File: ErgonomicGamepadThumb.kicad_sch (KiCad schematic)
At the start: 7 parts, among them J4 Conn_01x05, SW1 SW_DIP_x01, SW2 SW_DIP_x01, SW4 SW_DIP_x01

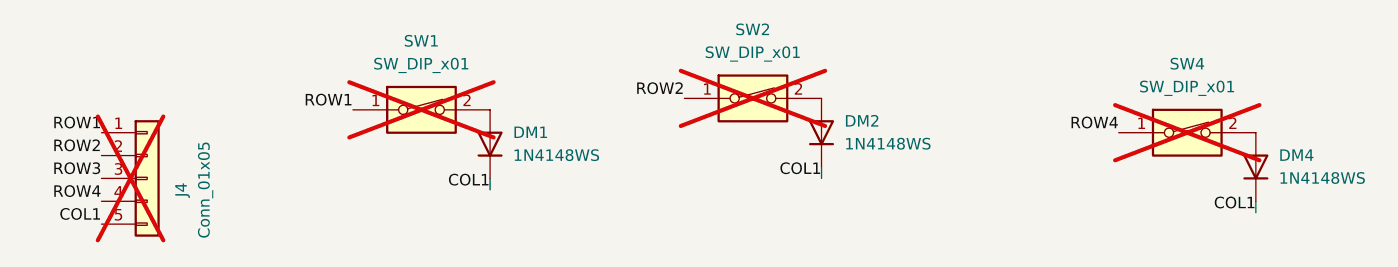
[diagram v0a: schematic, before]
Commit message: Continue ergonomic key stagger adjustments across satellite sheets
Update the layout-mirror script to read symbol positions from every
kicad_sch in the project, since the key matrix now lives across the
Pinkie/Thumb satellite sheets rather than a single top-level sheet.
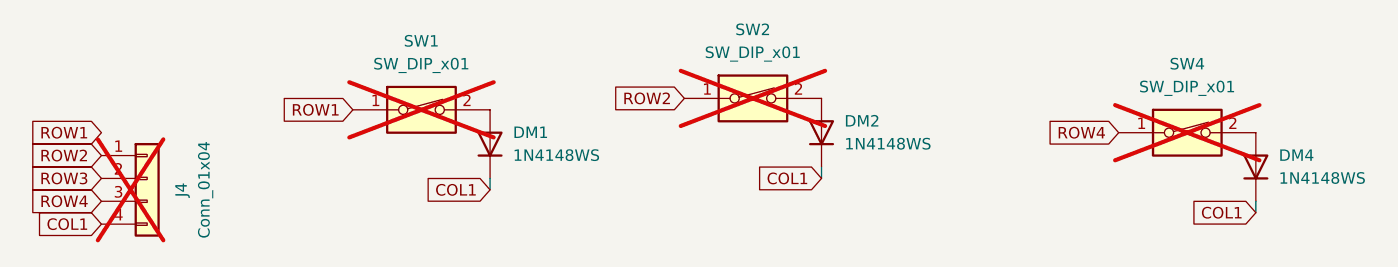
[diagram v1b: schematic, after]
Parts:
- J4: value Conn_01x05 -> Conn_01x04; footprint Connector_JST:JST_XH_B5B-XH-A_1x05_P2.50mm_Vertical -> Connector_JST:JST_XH_B4B-XH-A_1x04_P2.50mm_Vertical; symbol Connector_Generic:Conn_01x05 -> Connector_Generic:Conn_01x04; LCSC C157991 -> C144395; MPN B5B-XH-A(LF)(SN) -> B4B-XH-A(LF)(SN)
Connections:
- net COL1: now also J4.4 (Pin_4); no longer J4.5 (Pin_5)
- net ROW1: no longer J4.1 (Pin_1)
- net ROW2: now also J4.1 (Pin_1); no longer J4.2 (Pin_2)
- net ROW3: now also J4.2 (Pin_2); no longer J4.3 (Pin_3)
- net ROW4: now also J4.3 (Pin_3); no longer J4.4 (Pin_4)
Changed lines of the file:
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@@
 		)
 	)
-	(label "ROW4"
+	(global_label "ROW4"
+		(shape input)
 		(at 81.28 93.98 180)
-		(effects
-			(font
-				(size 1.27 1.27)
-			)
-			(justify right bottom)
-		)
-	)
-	(label "ROW3"
+		(fields_autoplaced yes)
+		(effects
+			(font
+				(size 1.27 1.27)
+			)
+			(justify right bottom)
+		)
+		(property "Intersheetrefs" "${INTERSHEET_REFS}"
+			(at 81.28 93.98 180)
+			(hide yes)
+			(show_name no)
+			(do_not_autoplace no)
+			(effects
+				(font
+					(size 1.27 1.27)
+				)
+				(justify right bottom)
+			)
+		)
+	)
+	(global_label "ROW3"
+		(shape input)
 		(at 81.28 91.44 180)
-		(effects
-			(font
-				(size 1.27 1.27)
-			)
-			(justify right bottom)
-		)
-	)
-	(label "COL1"
+		(fields_autoplaced yes)
+		(effects
+			(font
+				(size 1.27 1.27)
+			)
+			(justify right bottom)
+		)
+		(property "Intersheetrefs" "${INTERSHEET_REFS}"
+			(at 81.28 91.44 180)
+			(hide yes)
+			(show_name no)
+			(do_not_autoplace no)
+			(effects
+				(font
+					(size 1.27 1.27)
+				)
+				(justify right bottom)
+			)
+		)
+	)
+	(global_label "COL1"
+		(shape input)
 		(at 124.46 92.71 180)
-		(effects
-			(font
-				(size 1.27 1.27)
-			)
-			(justify right bottom)
-		)
-	)
-	(label "COL1"
+		(fields_autoplaced yes)
+		(effects
+			(font
+				(size 1.27 1.27)
+			)
+			(justify right bottom)
+		)
+		(property "Intersheetrefs" "${INTERSHEET_REFS}"
+			(at 124.46 92.71 180)
+			(hide yes)
+			(show_name no)
+			(do_not_autoplace no)
+			(effects
+				(font
+					(size 1.27 1.27)
+				)
+				(justify right bottom)
+			)
+		)
+	)
+	(global_label "COL1"
+		(shape input)
 		(at 81.28 96.52 180)
-		(effects
-			(font
-				(size 1.27 1.27)
-			)
-			(justify right bottom)
-		)
-	)
-	(label "ROW2"
+		(fields_autoplaced yes)
+		(effects
+			(font
+				(size 1.27 1.27)
+			)
+			(justify right bottom)
+		)
+		(property "Intersheetrefs" "${INTERSHEET_REFS}"
+			(at 81.28 96.52 180)
+			(hide yes)
+			(show_name no)
+			(do_not_autoplace no)
+			(effects
+				(font
+					(size 1.27 1.27)
+				)
+				(justify right bottom)
+			)
+		)
+	)
+	(global_label "ROW2"
+		(shape input)
 		(at 146.05 82.55 180)
-		(effects
-			(font
-				(size 1.27 1.27)
-			)
-			(justify right bottom)
-		)
-	)
-	(label "ROW1"
+		(fields_autoplaced yes)
+		(effects
+			(font
+				(size 1.27 1.27)
+			)
+			(justify right bottom)
+		)
+		(property "Intersheetrefs" "${INTERSHEET_REFS}"
+			(at 146.05 82.55 180)
+			(hide yes)
+			(show_name no)
+			(do_not_autoplace no)
+			(effects
+				(font
+					(size 1.27 1.27)
+				)
+				(justify right bottom)
+			)
+		)
+	)
+	(global_label "ROW1"
+		(shape input)
 		(at 81.28 86.36 180)
-		(effects
-			(font
-				(size 1.27 1.27)
-			)
-			(justify right bottom)
-		)
-	)
-	(label "COL1"
+		(fields_autoplaced yes)
+		(effects
+			(font
+				(size 1.27 1.27)
+			)
+			(justify right bottom)
+		)
+		(property "Intersheetrefs" "${INTERSHEET_REFS}"
+			(at 81.28 86.36 180)
+			(hide yes)
+			(show_name no)
+			(do_not_autoplace no)
+			(effects
+				(font
+					(size 1.27 1.27)
+				)
+				(justify right bottom)
+			)
+		)
+	)
+	(global_label "COL1"
+		(shape input)
 		(at 209.55 95.25 180)
-		(effects
-			(font
-				(size 1.27 1.27)
-			)
-			(justify right bottom)
-		)
-	)
-	(label "ROW4"
+		(fields_autoplaced yes)
+		(effects
+			(font
+				(size 1.27 1.27)
+			)
+			(justify right bottom)
+		)
+		(property "Intersheetrefs" "${INTERSHEET_REFS}"
+			(at 209.55 95.25 180)
+			(hide yes)
+			(show_name no)
+			(do_not_autoplace no)
+			(effects
+				(font
+					(size 1.27 1.27)
+				)
+				(justify right bottom)
+			)
+		)
+	)
+	(global_label "ROW4"
+		(shape input)
 		(at 194.31 86.36 180)
-		(effects
-			(font
-				(size 1.27 1.27)
-			)
-			(justify right bottom)
-		)
-	)
-	(label "ROW2"
+		(fields_autoplaced yes)
+		(effects
+			(font
+				(size 1.27 1.27)
+			)
+			(justify right bottom)
+		)
+		(property "Intersheetrefs" "${INTERSHEET_REFS}"
+			(at 194.31 86.36 180)
+			(hide yes)
+			(show_name no)
+			(do_not_autoplace no)
+			(effects
+				(font
+					(size 1.27 1.27)
+				)
+				(justify right bottom)
+			)
+		)
+	)
+	(global_label "ROW2"
+		(shape input)
 		(at 81.28 88.9 180)
-		(effects
-			(font
-				(size 1.27 1.27)
-			)
-			(justify right bottom)
-		)
-	)
-	(label "ROW1"
+		(fields_autoplaced yes)
+		(effects
+			(font
+				(size 1.27 1.27)
+			)
+			(justify right bottom)
+		)
+		(property "Intersheetrefs" "${INTERSHEET_REFS}"
+			(at 81.28 88.9 180)
+			(hide yes)
+			(show_name no)
+			(do_not_autoplace no)
+			(effects
+				(font
+					(size 1.27 1.27)
+				)
+				(justify right bottom)
+			)
+		)
+	)
+	(global_label "ROW1"
+		(shape input)
 		(at 109.22 83.82 180)
-		(effects
-			(font
-				(size 1.27 1.27)
-			)
-			(justify right bottom)
-		)
-	)
-	(label "COL1"
+		(fields_autoplaced yes)
+		(effects
+			(font
+				(size 1.27 1.27)
+			)
+			(justify right bottom)
+		)
+		(property "Intersheetrefs" "${INTERSHEET_REFS}"
+			(at 109.22 83.82 180)
+			(hide yes)
+			(show_name no)
+			(do_not_autoplace no)
+			(effects
+				(font
+					(size 1.27 1.27)
+				)
+				(justify right bottom)
+			)
+		)
+	)
+	(global_label "COL1"
+		(shape input)
 		(at 161.29 91.44 180)
-		(effects
-			(font
-				(size 1.27 1.27)
-			)
-			(justify right bottom)
+		(fields_autoplaced yes)
+		(effects
+			(font
+				(size 1.27 1.27)
+			)
+			(justify right bottom)
+		)
+		(property "Intersheetrefs" "${INTERSHEET_REFS}"
+			(at 161.29 91.44 180)
+			(hide yes)
+			(show_name no)
+			(do_not_autoplace no)
+			(effects
+				(font
+					(size 1.27 1.27)
+				)
+				(justify right bottom)
+			)
 		)
 	)
 	(symbol
-		(lib_id "Connector_Generic:Conn_01x05")
+		(lib_id "Connector_Generic:Conn_01x04")
 		(at 86.36 91.44 0)
 		(unit 1)
@@
 			)
 		)
-		(property "Value" "Conn_01x05"
+		(property "Value" "Conn_01x04"
 			(at 92.71 92.71 90)
 			(show_name no)
@@
 			)
 		)
-		(property "Footprint" "Connector_JST:JST_XH_B5B-XH-A_1x05_P2.50mm_Vertical"
-			(at 86.36 91.44 0)
-			(hide yes)
-			(show_name no)
-			(do_not_autoplace no)
-			(effects
-				(font
-					(size 1.27 1.27)
-				)
-			)
-		)
-		(property "Datasheet" "https://www.lcsc.com/datasheet/C157991.pdf"
-			(at 86.36 91.44 0)
-			(hide yes)
-			(show_name no)
-			(do_not_autoplace no)
-			(effects
-				(font
-					(size 1.27 1.27)
-				)
-			)
-		)
-		(property "Description" "Generic connector, single row, 01x05, script generated (kicad-library-utils/schlib/autogen/connector/)"
+		(property "Footprint" "Connector_JST:JST_XH_B4B-XH-A_1x04_P2.50mm_Vertical"
+			(at 86.36 91.44 0)
+			(hide yes)
+			(show_name no)
+			(do_not_autoplace no)
+			(effects
+				(font
+					(size 1.27 1.27)
+				)
+			)
+		)
+		(property "Datasheet" "https://www.lcsc.com/datasheet/C144395.pdf"
+			(at 86.36 91.44 0)
+			(hide yes)
+			(show_name no)
+			(do_not_autoplace no)
+			(effects
+				(font
+					(size 1.27 1.27)
+				)
+			)
+		)
+		(property "Description" "Generic connector, single row, 01x04, script generated (kicad-library-utils/schlib/autogen/connector/)"
 			(at 86.36 91.44 0)
 			(hide yes)
@@
 			)
 		)
-		(property "MPN" "B5B-XH-A(LF)(SN)"
+		(property "MPN" "B4B-XH-A(LF)(SN)"
 			(at 86.36 91.44 0)
 			(hide yes)
@@
 			)
 		)
-		(property "LCSC" "C157991"
-			(at 86.36 91.44 0)
-			(hide yes)
-			(show_name no)
-			(do_not_autoplace no)
-			(effects
-				(font
-					(size 1.27 1.27)
-				)
-			)
-		)
-		(pin "5"
+		(property "LCSC" "C144395"
+			(at 86.36 91.44 0)
+			(hide yes)
+			(show_name no)
+			(do_not_autoplace no)
+			(effects
+				(font
+					(size 1.27 1.27)
+				)
+			)
 		)
 		(pin "1"
